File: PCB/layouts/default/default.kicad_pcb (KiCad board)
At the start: 2 copper layers, 68 parts

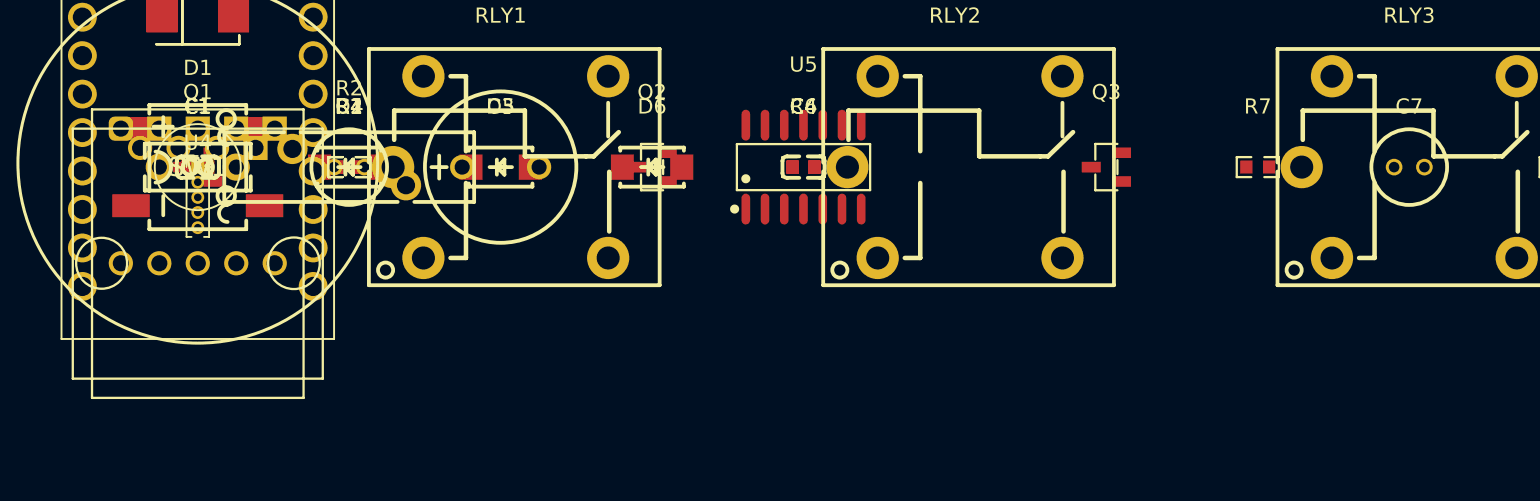
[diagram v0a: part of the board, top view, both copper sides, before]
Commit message: Swapped buck converter
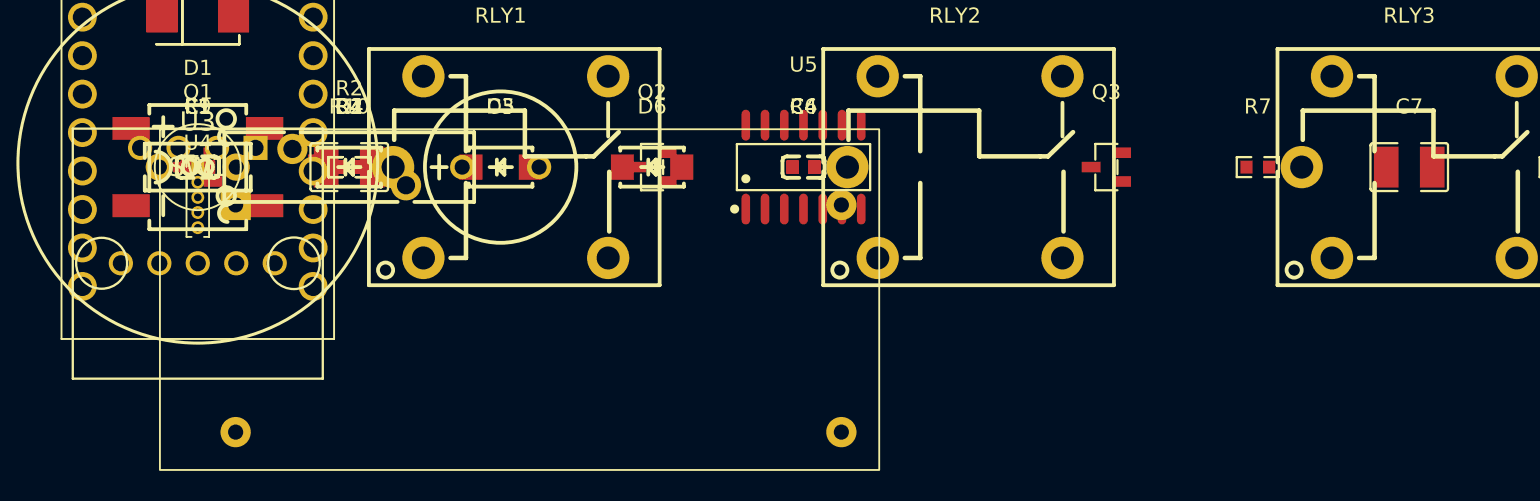
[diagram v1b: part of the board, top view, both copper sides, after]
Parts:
- added R10: 100kΩ ±1% 100mW, UNI_ROYAL_0603WAF1003T5E:R0603, F.Cu at (10.0, 0.00)
- added R9: 10kΩ ±1% 100mW, UNI_ROYAL_0603WAF1002T5E:R0603, F.Cu at (0.00, 0.00)
- C2, C7: value 100µF ±20% 16V -> 100µF ±20% 16V X5R; footprint KNSCHA_01EC1385:CAP-TH_BD5.0-P2.00-D0.5-FD-1 -> Chinocera_HGC1210R5107M160NSVK:C1210
- R2: footprint Hongzhi_Elec_14D330K:RES-TH_L16.5-W4.6-P7.50-D0.8-S2.40 -> Hongzhi_Elec_14D470K:RES-TH_L16.5-W4.6-P7.50-D0.8-S2.40
- U3: footprint DROK_Buck:DROK_BUCK -> LM2596_board:LM2596_bord
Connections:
- C3 pad 1: enable -> vin_plus
- D1 pad 1: enable -> vin_plus
- D3 pad 1: enable -> vin_plus
- U3 pad IN+: enable -> vin_plus

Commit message: Started on layout
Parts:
- R10: value 100kΩ ±1% 100mW -> 1kΩ ±1% 100mW; footprint UNI_ROYAL_0603WAF1003T5E:R0603 -> UNI_ROYAL_0603WAF1001T5E:R0603
- R4: value 1kΩ ±1% 100mW -> 10kΩ ±1% 100mW; footprint UNI_ROYAL_0603WAF1001T5E:R0603 -> UNI_ROYAL_0603WAF1002T5E:R0603
- R7: value 1kΩ ±1% 100mW -> 100kΩ ±1% 100mW; footprint UNI_ROYAL_0603WAF1001T5E:R0603 -> UNI_ROYAL_0603WAF1003T5E:R0603
- R9: value 10kΩ ±1% 100mW -> 1kΩ ±1% 100mW; footprint UNI_ROYAL_0603WAF1002T5E:R0603 -> UNI_ROYAL_0603WAF1001T5E:R0603
- U3: moved to B.Cu
- moved C10 295.9 mm to (-17.4, 95.9)
- moved C11 295.9 mm to (-7.45, 95.9)
- moved C12 295.9 mm to (42.5, 95.9)
- moved C13 295.9 mm to (52.5, 95.9)
- moved C14 295.9 mm to (62.5, 95.9)
- moved C15 295.9 mm to (72.5, 95.9)
- moved C16 295.9 mm to (82.5, 95.9)
- moved C17 295.9 mm to (92.5, 95.9)
- moved C18 295.9 mm to (102.5, 95.9)
- moved C19 295.9 mm to (112.5, 95.9)
- moved C20 295.9 mm to (2.55, 95.9)
- moved C21 295.9 mm to (12.6, 95.9)
- moved C22 295.9 mm to (22.6, 95.9)
- moved C23 295.9 mm to (32.5, 95.9)
- moved LED1 295.9 mm to (-17.4, 92.8)
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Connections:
- R10 pad 1: vin_plus -> spi0_cs-control
- R10 pad 2: buck_enable -> bleed_res-a-2
- R4 pad 1: spi0_sclk-control -> buck_enable
- R4 pad 2: bleed_res-a-0 -> power-GND
- R7 pad 1: spi0_cs-control -> vin_plus
- R7 pad 2: bleed_res-a-2 -> buck_enable
- R9 pad 1: buck_enable -> spi0_sclk-control
- R9 pad 2: power-GND -> bleed_res-a-0

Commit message: Started placement and examined components
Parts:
- removed C2, C7: 100µF ±20% 16V X5R, Chinocera_HGC1210R5107M160NSVK:C1210
- removed C8, C9: 100nF ±10% 50V X7R, YAGEO_CC0603KRX7R9BB104:C0603
- removed R1, R13, R14, R15: 10kΩ ±1% 100mW, UNI_ROYAL_0603WAF1002T5E:R0603
- removed R11, R8: 100kΩ ±1% 100mW, UNI_ROYAL_0603WAF1003T5E:R0603
- removed R16, R17: 4.7kΩ ±1% 100mW, UNI_ROYAL_0603WAF4701T5E:R0603
- removed R3: 330Ω ±1% 100mW, UNI_ROYAL_0603WAF3300T5E:R0603
- R4: value 10kΩ ±1% 100mW -> 100kΩ ±1% 100mW; footprint UNI_ROYAL_0603WAF1002T5E:R0603 -> UNI_ROYAL_0603WAF1003T5E:R0603
- moved R7 236.1 mm to (207.8, 129.0)
- moved R10 224.1 mm to (214.0, 128.0)
- moved R4 208.1 mm to (164.5, 127.5), turned to 180 degrees
- moved R9 196.3 mm to (169.2, 127.5)
- moved C1 183.3 mm to (242.0, 73.0), turned to 90 degrees
- moved U5 77.0 mm to (135.2, 80.3), turned to 0 degrees
- moved R6 75.8 mm to (192.0, 129.5)
- moved U1 64.7 mm to (251.8, 92.5)
- moved R5 62.3 mm to (188.5, 129.5)
- moved U2 46.1 mm to (231.5, 79.5)
- moved D4 43.5 mm to (157.5, 112.5), turned to -90 degrees
- moved D6 39.8 mm to (198.0, 111.5), turned to -90 degrees
- moved D5 31.9 mm to (177.5, 111.5), turned to -90 degrees
- moved SW1 24.9 mm to (239.0, 112.5)
- moved C4 24.8 mm to (246.5, 92.3), turned to -90 degrees
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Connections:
- net gpio[5]-b renamed b
- net gpio[6]-a renamed sw
- R4 pad 1: buck_enable -> bleed_res-a-0
- R5 pad 1: bleed_res-a-0 -> bleed_res-a-1
- R7 pad 1: vin_plus -> bleed_res-a-2
- R7 pad 2: buck_enable -> power-GND
- U2 pad 0: gpio[0]-b -> gpio[0]-line
